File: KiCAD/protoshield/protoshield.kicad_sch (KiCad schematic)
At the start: 30 parts, among them J1 Screw_Terminal_01x03, J2 Screw_Terminal_01x02, J3 Screw_Terminal_01x02, J4 Screw_Terminal_01x02, J5 Screw_Terminal_01x02, J6 Screw_Terminal_01x03, J7 Screw_Terminal_01x03, U2 Metro_ESP32S3

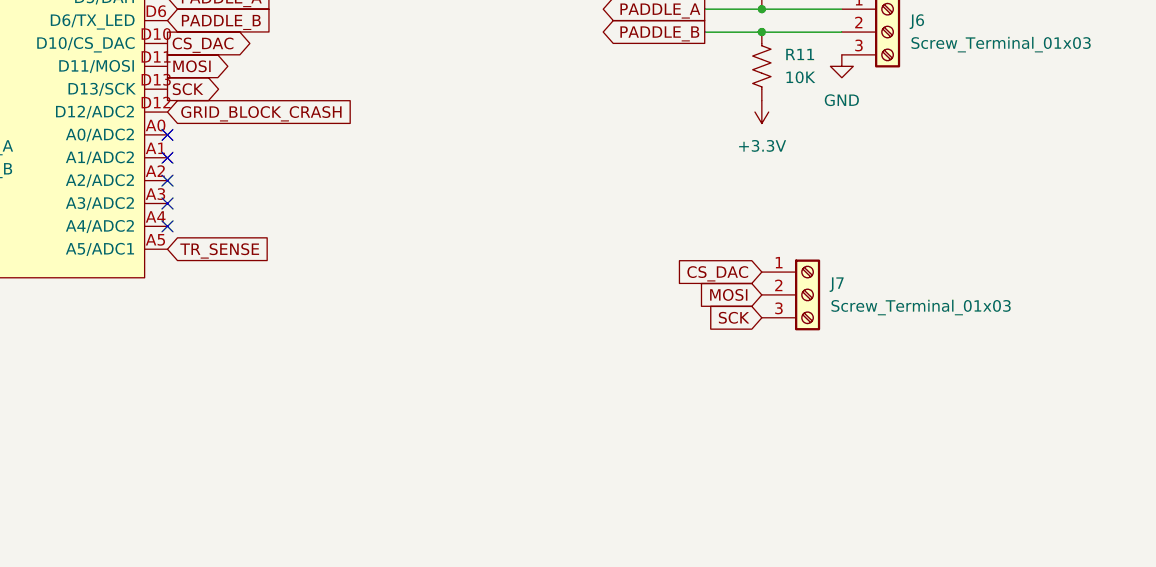
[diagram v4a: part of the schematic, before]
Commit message: revB frozen state: MCP4922 swap + LDAC decouple + sheet rename + protoshield work
Captures the in-flight state of revB at the point where the project pivoted
to a full-SS output stage on a new branch (SS_Rev_C, cut from this commit).
revB is retained as a fallback if the SS PA plan on revC proves inadequate.

Included changes:
- Analog: MCP4921 (single DAC) replaced with MCP4922 (dual DAC). Channel
  assignment: DAC_A -> PA_OUTPUT_LEVEL (new global label, awaiting PA
  board), DAC_B -> Gate 2 (DGFET envelope keyer). Channels swapped from
  initial-design intent for layout convenience.
- Analog: DAC_LDAC_N decoupled from PCF8575 P5 (that global label renamed
  to PCF_P5_SPARE). Intent: route LDAC to Metro A4 for zero-latency
  simultaneous-DAC-update capability. Physical route to A4 NOT yet added
  -- DAC_LDAC_N label on dac.kicad_sch is dangling and will fail ERC.
- Analog: KiCad-driven used_designators bookkeeping (analog.kicad_pro).
- Sheet rename: KiCAD/analog/untitled.kicad_sch -> dac.kicad_sch. Root
  schematic Sheetfile reference updated.
- Protoshield: 537 lines of additions to protoshield.kicad_sch (user
  work). Not reviewed in this commit -- carried forward as-is.
- .gitignore: added tools/_*.py exclusion (local review-helper scripts).

**revB is NOT fab-ready in this state.** See memory
project_revB_pre_fab_check.md (outside repo) for the punch list. If the
SS PA plan ever reverses and someone revives revB, ALL open items must
be closed and a full pass through Documentation/pcb_fab_checklist.md
must be completed before any gerber submit.

Co-Authored-By: Claude Opus 4.7 <noreply@anthropic.com>
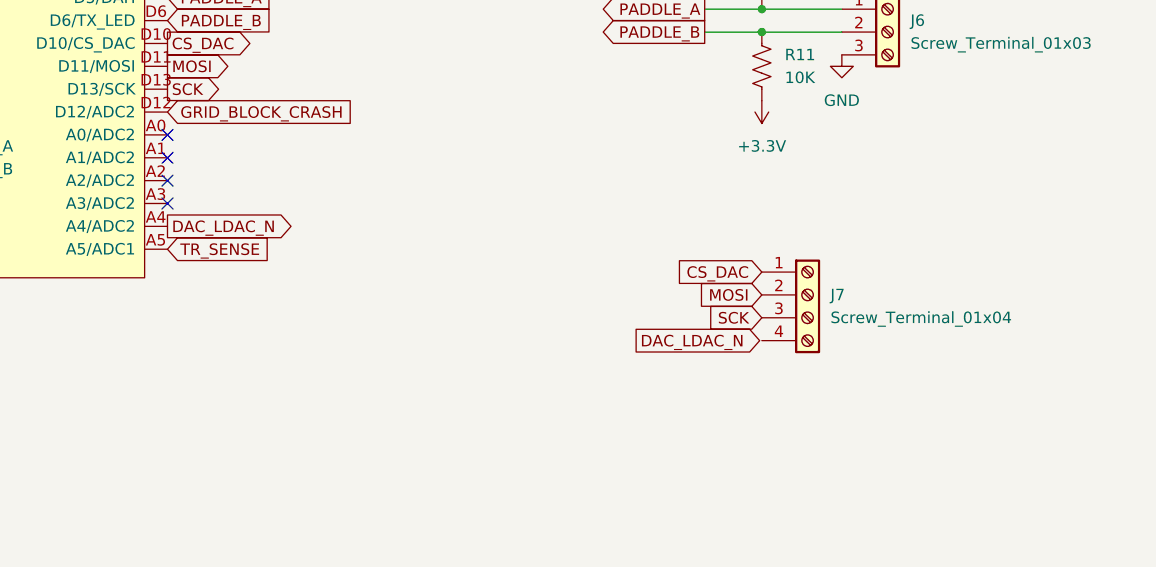
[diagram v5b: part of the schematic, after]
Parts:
- removed J7: Screw_Terminal_01x03, TerminalBlock_Phoenix:TerminalBlock_Phoenix_MKDS-1,5-3_1x03_P5.00mm_Horizontal, symbol Connector:Screw_Terminal_01x03
- added J7: Screw_Terminal_01x04, symbol Connector:Screw_Terminal_01x04
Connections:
- net CS_DAC: now also J7.1 (Pin_1)
- net MOSI: now also J7.2 (Pin_2)
- net SCK: now also J7.3 (Pin_3)
- net DAC_LDAC_N: now reaches U2.A4 (A4/ADC2)
- no-connect marks 9 -> 8
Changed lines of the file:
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@@
 	)
 	(no_connect
-		(at 161.29 96.52)
-	)
-	(no_connect
 		(at 161.29 93.98)
 	)
@@
 		)
 	)
+	(global_label "DAC_LDAC_N"
+		(shape output)
+		(at 213.36 109.22 0)
+		(fields_autoplaced yes)
+		(effects
+			(font
+				(size 1.27 1.27)
+			)
+			(justify left)
+		)
+		(property "Intersheetrefs" "${INTERSHEET_REFS}"
+			(at 227.8962 109.22 0)
+			(hide yes)
+			(show_name no)
+			(do_not_autoplace no)
+			(effects
+				(font
+					(size 1.27 1.27)
+				)
+				(justify left)
+			)
+		)
+	)
 	(global_label "RESET_N"
 		(shape output)
@@
 		)
 	)
+	(global_label "DAC_LDAC_N"
+		(shape output)
+		(at 161.29 96.52 0)
+		(fields_autoplaced yes)
+		(effects
+			(font
+				(size 1.27 1.27)
+			)
+			(justify left)
+		)
+		(property "Intersheetrefs" "${INTERSHEET_REFS}"
+			(at 175.8262 96.52 0)
+			(hide yes)
+			(show_name no)
+			(do_not_autoplace no)
+			(effects
+				(font
+					(size 1.27 1.27)
+				)
+				(justify left)
+			)
+		)
+	)
 	(global_label "LDAC_4728"
 		(shape output)
@@
 	)
 	(symbol
+		(lib_id "Connector:Screw_Terminal_01x04")
+		(at 232.41 104.14 0)
+		(unit 1)
+		(body_style 1)
+		(exclude_from_sim no)
+		(in_bom yes)
+		(on_board yes)
+		(in_pos_files yes)
+		(dnp no)
+		(fields_autoplaced yes)
+		(property "Reference" "J7"
+			(at 234.95 104.1399 0)
+			(show_name no)
+			(do_not_autoplace no)
+			(effects
+				(font
+					(size 1.27 1.27)
+				)
+				(justify left)
+			)
+		)
+		(property "Value" "Screw_Terminal_01x04"
+			(at 234.95 106.6799 0)
+			(show_name no)
+			(do_not_autoplace no)
+			(effects
+				(font
+					(size 1.27 1.27)
+				)
+				(justify left)
+			)
+		)
+		(property "Footprint" ""
+			(at 232.41 104.14 0)
+			(hide yes)
+			(show_name no)
+			(do_not_autoplace no)
+			(effects
+				(font
+					(size 1.27 1.27)
+				)
+			)
+		)
+		(property "Datasheet" ""
+			(at 232.41 104.14 0)
+			(hide yes)
+			(show_name no)
+			(do_not_autoplace no)
+			(effects
+				(font
+					(size 1.27 1.27)
+				)
+			)
+		)
+		(property "Description" "Generic screw terminal, single row, 01x04, script generated (kicad-library-utils/schlib/autogen/connector/)"
+			(at 232.41 104.14 0)
+			(hide yes)
+			(show_name no)
+			(do_not_autoplace no)
+			(effects
+				(font
+					(size 1.27 1.27)
+				)
+			)
+		)
+		(pin "3"
+		)
+		(pin "4"
+		)
+		(pin "2"
+		)
+		(pin "1"
+		)
+		(instances
+			(project "protoshield"
+				(path "/90f14230-179e-419d-8d57-3db6b8a7c39f"
+					(reference "J7")
+					(unit 1)
+				)
+			)
+		)
+	)
+	(symbol
 		(lib_id "power:GND")
 		(at 43.18 168.91 0)
@@
 					(unit 1)
 				)
-			)
-		)
-	)
-	(symbol
-		(lib_id "Connector:Screw_Terminal_01x03")
-		(at 232.41 104.14 0)
-		(unit 1)
-		(body_style 1)
-		(exclude_from_sim no)
-		(in_bom yes)
-		(on_board yes)
-		(in_pos_files yes)
-		(dnp no)
-		(fields_autoplaced yes)
-		(property "Reference" "J7"
-			(at 234.95 102.8699 0)
-			(show_name no)
-			(do_not_autoplace no)
-			(effects
-				(font
-					(size 1.27 1.27)
-				)
-				(justify left)
-			)
-		)
-		(property "Value" "Screw_Terminal_01x03"
-			(at 234.95 105.4099 0)
-			(show_name no)
-			(do_not_autoplace no)
-			(effects
-				(font
-					(size 1.27 1.27)
-				)
-				(justify left)
-			)
-		)
-		(property "Footprint" "TerminalBlock_Phoenix:TerminalBlock_Phoenix_MKDS-1,5-3_1x03_P5.00mm_Horizontal"
-			(at 232.41 104.14 0)
-			(hide yes)
-			(show_name no)
-			(do_not_autoplace no)
-			(effects
-				(font
-					(size 1.27 1.27)
-				)
-			)
-		)
-		(property "Datasheet" ""
-			(at 232.41 104.14 0)
-			(hide yes)
-			(show_name no)
-			(do_not_autoplace no)
-			(effects
-				(font
-					(size 1.27 1.27)
-				)
-			)
-		)
-		(property "Description" "Generic screw terminal, single row, 01x03, script generated (kicad-library-utils/schlib/autogen/connector/)"
-			(at 232.41 104.14 0)
-			(hide yes)
-			(show_name no)
-			(do_not_autoplace no)
-			(effects
-				(font
-					(size 1.27 1.27)
-				)
-			)
-		)
-		(pin "2"
-		)
-		(pin "1"
-		)
-		(pin "3"
-		)
-		(instances
-			(project "protoshield"
-				(path "/90f14230-179e-419d-8d57-3db6b8a7c39f"
-					(reference "J7")
-					(unit 1)
-				)

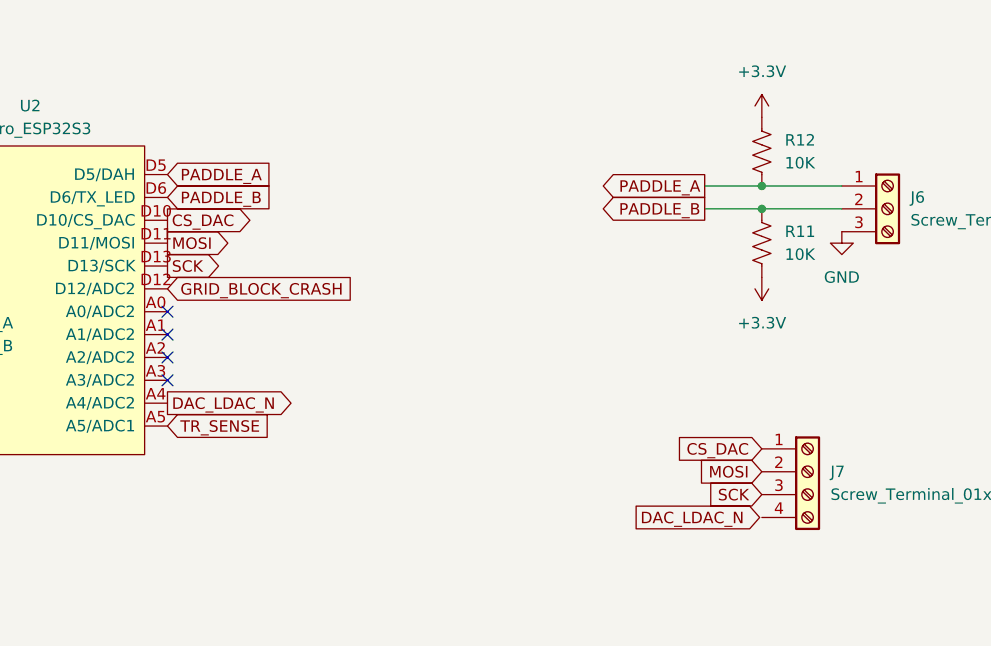
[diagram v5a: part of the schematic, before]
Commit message: KiCad revC: ss_pa pa_stage initial draft + protoshield additions
ss_pa:
- First pass on pa_stage.kicad_sch: Q1/Q2 push-pull FETs, T1 output
  transformer, T2 drain-feed transformer, C3 drain snubber,
  per-FET source sense (2x 0.22R parallel per FET = 0.11R to GND)
  with Source_Sense_A/B taps, J1 coax output
- Known pending (per user): bias network, input DC-block caps,
  drain-gate feedback networks, +13.8V bulk electrolytic
- Known issues flagged in review (to be fixed on next edit):
  Q1/Q2 are IRF540N (should be IRF510 — gate capacitance mismatch),
  T2 phasing (both corresponding ends at CT → parallel winding
  instead of push-pull), no RFC between +13.8V and T2 CT
- First netlist export captured (ss_pa.net)

protoshield:
- Added capacitors C2-C3, resistors R1-R2, power symbols
  (#PWR5, #PWR22-24)

Co-Authored-By: Claude Opus 4.7 <noreply@anthropic.com>
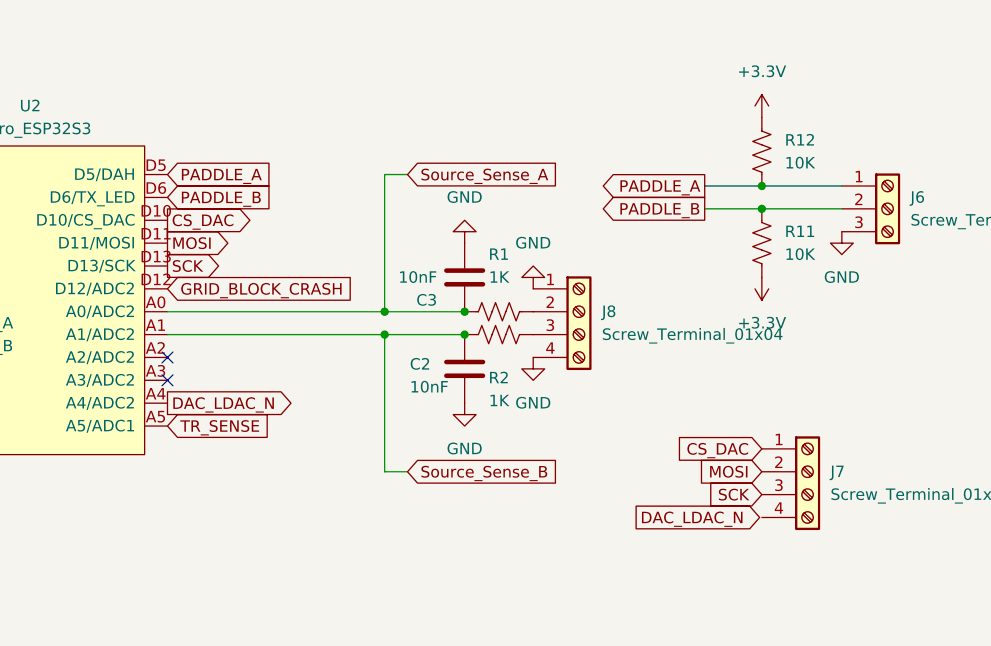
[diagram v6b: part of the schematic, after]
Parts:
- added C2, C3: 10nF, symbol Device:C
- added J8: Screw_Terminal_01x04, symbol Connector:Screw_Terminal_01x04
- added R1, R2: 1K, symbol Device:R_US
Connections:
- net GND: now also C2.2, C3.2, J8.1 (Pin_1), J8.4 (Pin_4)
- net Source_Sense_A: now reaches U2.A0 (A0/ADC2)
- net Source_Sense_A: now also C3.1, R1.1
- net Source_Sense_B: now reaches U2.A1 (A1/ADC2)
- net Source_Sense_B: now also C2.1, R2.1
- new net: J8.3 (Pin_3), R2.2
- new net: J8.2 (Pin_2), R1.2
- no-connect marks 8 -> 6
